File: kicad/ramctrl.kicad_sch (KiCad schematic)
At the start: 32 parts, among them U10 74LS245, U12 74S280, U55 74S158, U56 74S158, U71 74S157, U72 74S08, U73 74LS04, U87 74S08, U88 74S138, U89 74S138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

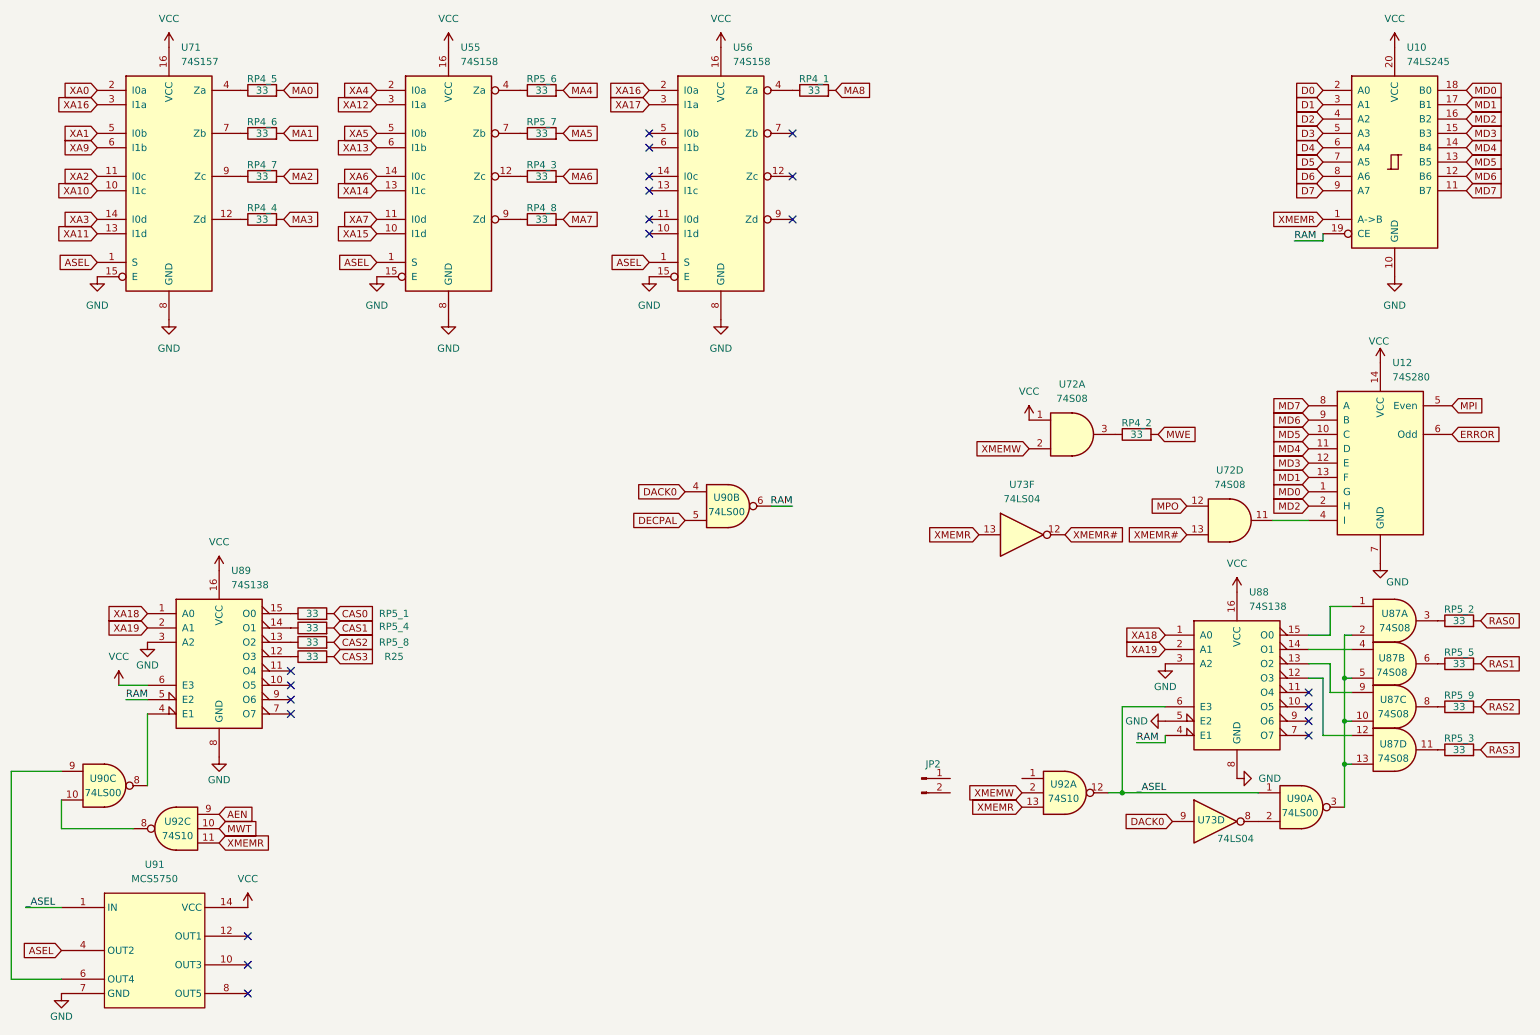
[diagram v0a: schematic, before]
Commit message: finalized schematic
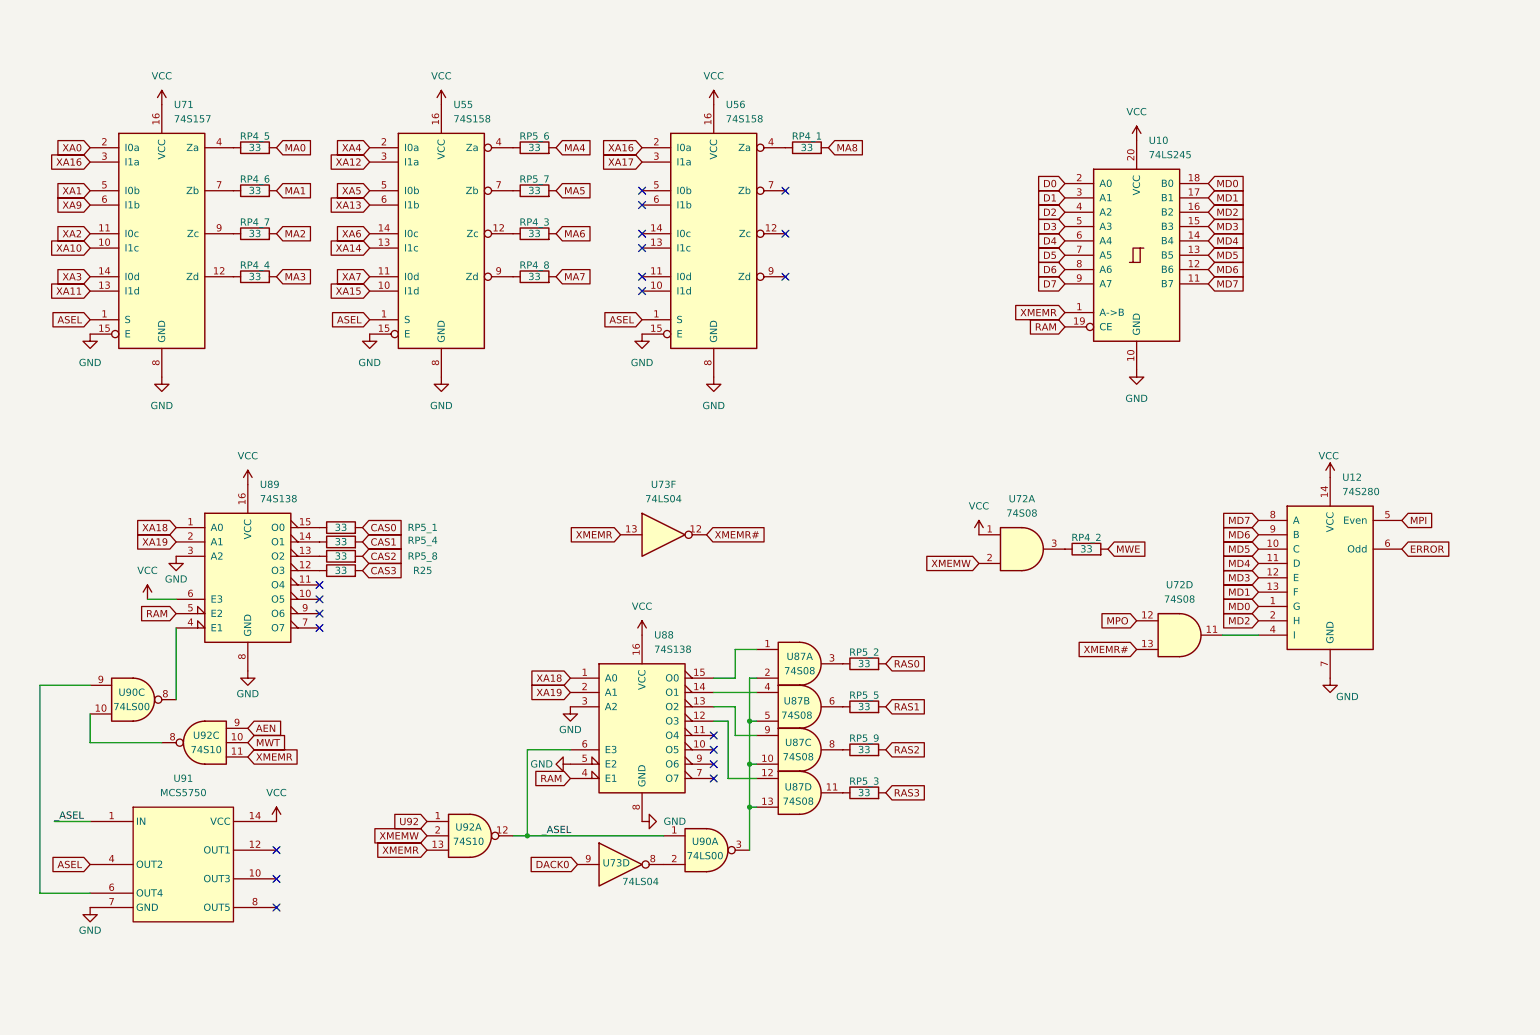
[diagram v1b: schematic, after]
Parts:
- removed JP2: Conn_01x02_Pin, symbol Connector:Conn_01x02_Pin
- removed unit 2 of U90
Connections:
- net U92: now reaches U92.1
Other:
- moved on the sheet: R25, RP4_1, RP4_2, RP4_3, RP4_4, RP4_5, RP4_6, RP4_7, RP4_8, RP5_1, RP5_2, RP5_3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
